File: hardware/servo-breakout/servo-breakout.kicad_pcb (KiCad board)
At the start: 2 copper layers, 89.3 x 41.1 mm, 20 parts, among them J1 Servos 1-4, J2 Servos 5-8, M1 Servo 1, M2 Servo 2, M3 Servo 3, M4 Servo 4, M5 Servo 5, M6 Servo 6, M7 Servo 7, M8 Servo 8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

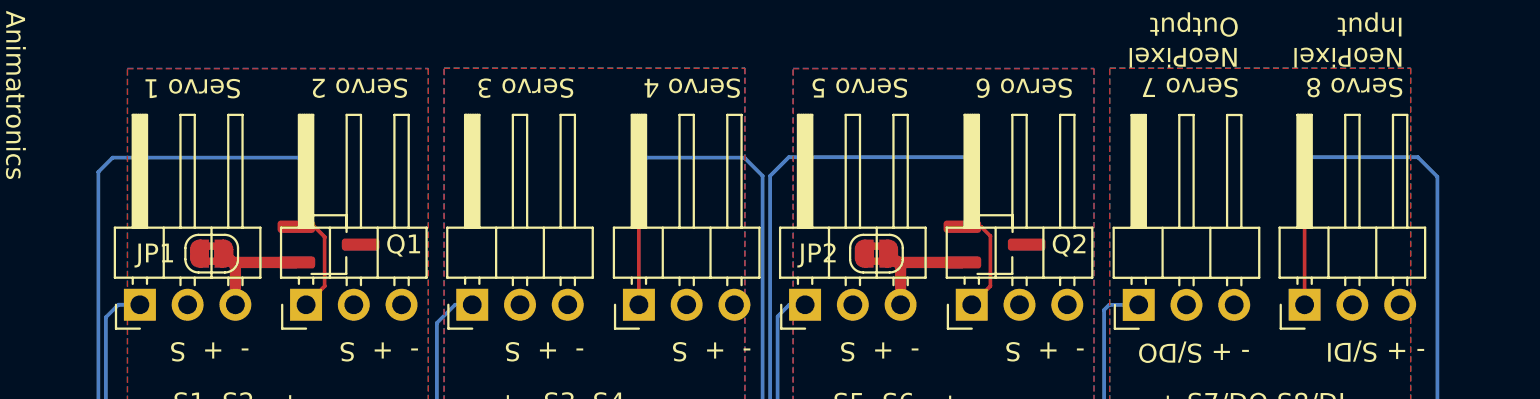
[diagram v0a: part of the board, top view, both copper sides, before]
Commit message: Rev 1.1: - Update to latest KiCad - Fixed short in servo board - Updates to right-angle diag connector on servo boards - Fixed microproc footprint on diag board - Flipped I2C connector to top of diag board - Pass all ERC and DRC checks, add exclusions
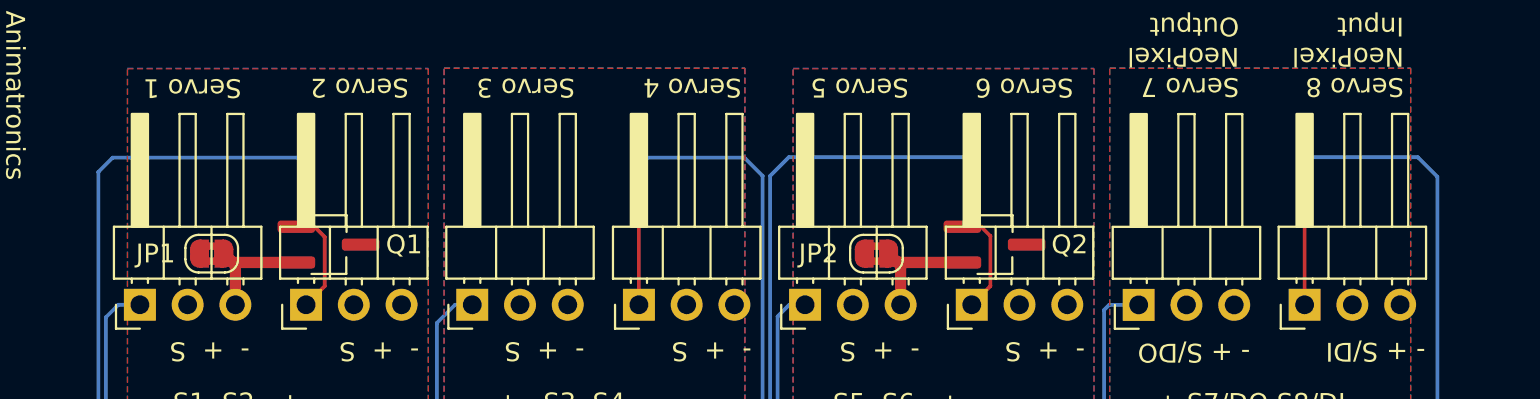
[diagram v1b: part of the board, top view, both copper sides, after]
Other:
- board text added: "ANI-SBO, Rev 1.1 Sparky Bobo Designs"
- board text removed: "ANI-SBO, Rev 1.0 Sparky Bobo Designs"
